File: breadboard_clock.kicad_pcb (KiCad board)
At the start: 2 copper layers, 54 x 53.5 mm, 42 parts, among them J1 Conn_01x02_Male, J2 Conn_01x03_Male, J3 USB_C_Receptacle_USB2.0, P1 1M, SW1 SW_Push, SW2 SW_SPDT, U1 ICM7555, U2 74LS04-Full, U3 74LS08-Full, U5 ICM7555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

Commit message: Add files via upload
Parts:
- added G***: LOGO, breadboard_clock-master:github_image, B.Cu at (467.5, 80.0)
- added REF**: MountingHole_2.5mm, MountingHole:MountingHole_2.5mm, F.Cu at (222.0, 78.0)
- added REF**: MountingHole_2.5mm, MountingHole:MountingHole_2.5mm, F.Cu at (222.0, 122.0)
- added REF**: MountingHole_2.5mm, MountingHole:MountingHole_2.5mm, F.Cu at (178.0, 122.0)
- added REF**: MountingHole_2.5mm, MountingHole:MountingHole_2.5mm, F.Cu at (178.0, 78.0)
- P1: footprint Potentiometer_SMD:Potentiometer_Bourns_3224X_Vertical -> Potentiometer_SMD:Potentiometer_Bourns_3314J_Vertical
- SW1: footprint Button_Switch_SMD:SW_SPST_B3S-1000 -> Button_Switch_SMD:SW_SPST_B3U-1100P-B
- moved J2 74.5 mm to (221.1, 114.5)
- moved P1 73.8 mm to (193.5, 115.5)
- moved R2 73.8 mm to (189.2, 115.6)
- moved SW1 67.6 mm to (205.5, 115.2)
- moved C8 65.0 mm to (201.9, 88.0), turned to 0 degrees
- moved U3 64.6 mm to (210.0, 82.5)
- moved C6 64.6 mm to (215.0, 81.5)
- moved D5 61.3 mm to (180.2, 88.5)
- moved C9 61.1 mm to (198.1, 88.0)
- moved C10 60.8 mm to (223.5, 88.5)
- moved U2 60.5 mm to (218.5, 89.5)
- moved D4 59.8 mm to (196.8, 99.6)
- moved C1 59.8 mm to (183.7, 105.0)
- moved C5 59.8 mm to (206.5, 102.9)
- moved D1 59.8 mm to (178.5, 99.5)
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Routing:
- net GND: track 160.8 -> 239.1 mm, vias 16 -> 20
- net CLK: track 29.1 -> 75.8 mm, vias 0 -> 2
- net VCC: track 33.3 -> 70.4 mm, vias 8 -> 13
- net Net-(D1-Pad2): track 35.9 -> 50.2 mm
- net Net-(R4-Pad2): track 39.5 -> 25.2 mm
- net Net-(D4-Pad2): track 38.2 -> 49.3 mm
- net Net-(U2-Pad6): track 14.2 -> 23.9 mm, vias 0 -> 2
- net Net-(R8-Pad2): track 24.4 -> 33.0 mm
- net Net-(C4-Pad1): track 16.7 -> 10.3 mm, vias 2 -> 0
- net ~CLK: track 58.9 -> 52.8 mm, vias 0 -> 2
- net Net-(U2-Pad2): track 21.7 -> 15.7 mm
- net Net-(R1-Pad2): track 26.9 -> 21.5 mm, vias 0 -> 2
- net Net-(U2-Pad3): track 13.0 -> 17.2 mm, vias 2 -> 0
- net Net-(U2-Pad11): track 17.0 -> 20.0 mm
- net Net-(U2-Pad4): track 10.7 -> 13.7 mm
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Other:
- board size 54 x 53.5 mm -> 50 x 50 mm
- board text added: "555 TIMER CLOCK DESIGNED BY b0xmaker github.com/b0xmaker/breadboard_clock v0: PCB CREATED 2021-06-20"
- board text added: "AND GATE"
- board text added: "AUTO CLK (.5-7 Hz)"
- board text added: "CLK ADV. (MAN)"
- board text added: "CLK SPEED (AUTO)"
- board text added: "CLK SWITCH (MAN/AUTO)"
- board text added: "INVERTER"
- board text added: "MAN CLK"
- board text added: "POWER INPUT (2-18V DC)"
- board text added: "USB C INPUT"

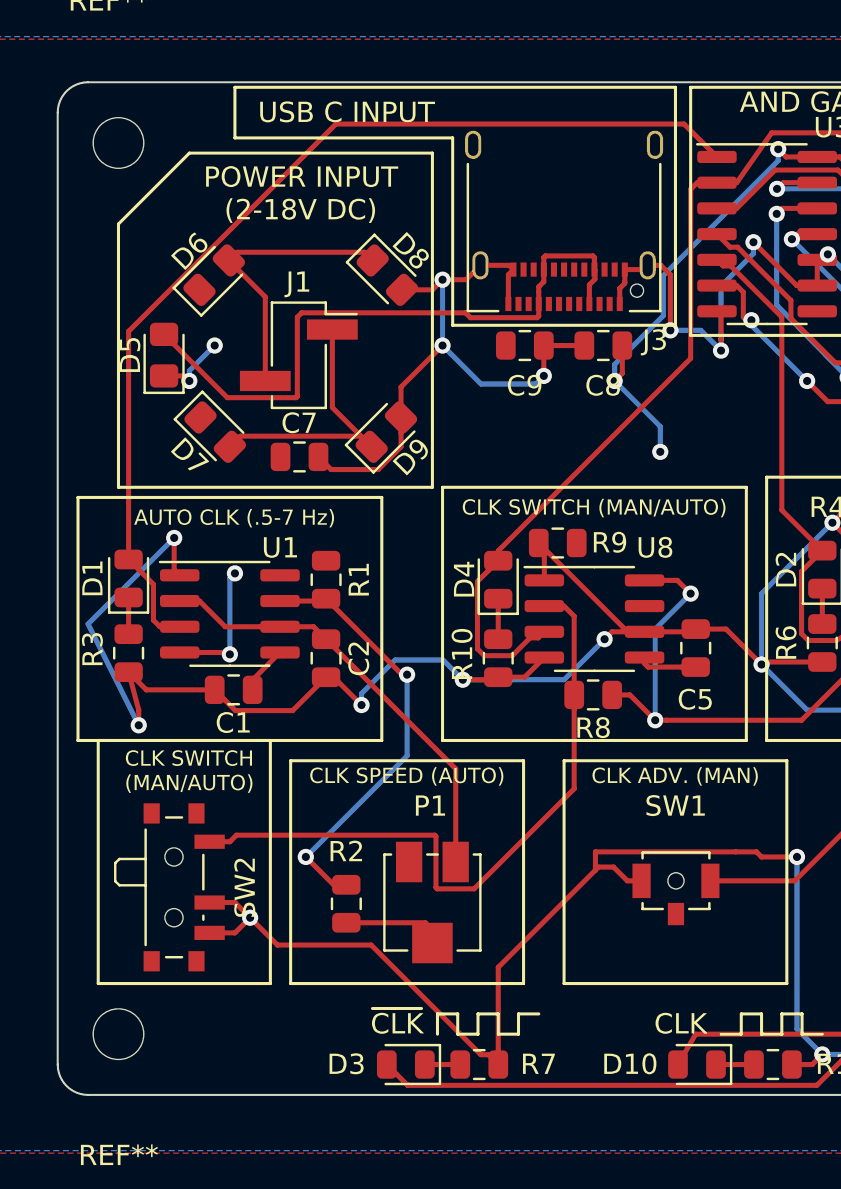
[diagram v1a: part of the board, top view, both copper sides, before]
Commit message: Add files via upload
Modified PCB/Schematic to get clock switching 555 circuit working. Trace was leading from pin 4 to GND, causing this 555 to always be in "reset" mode.
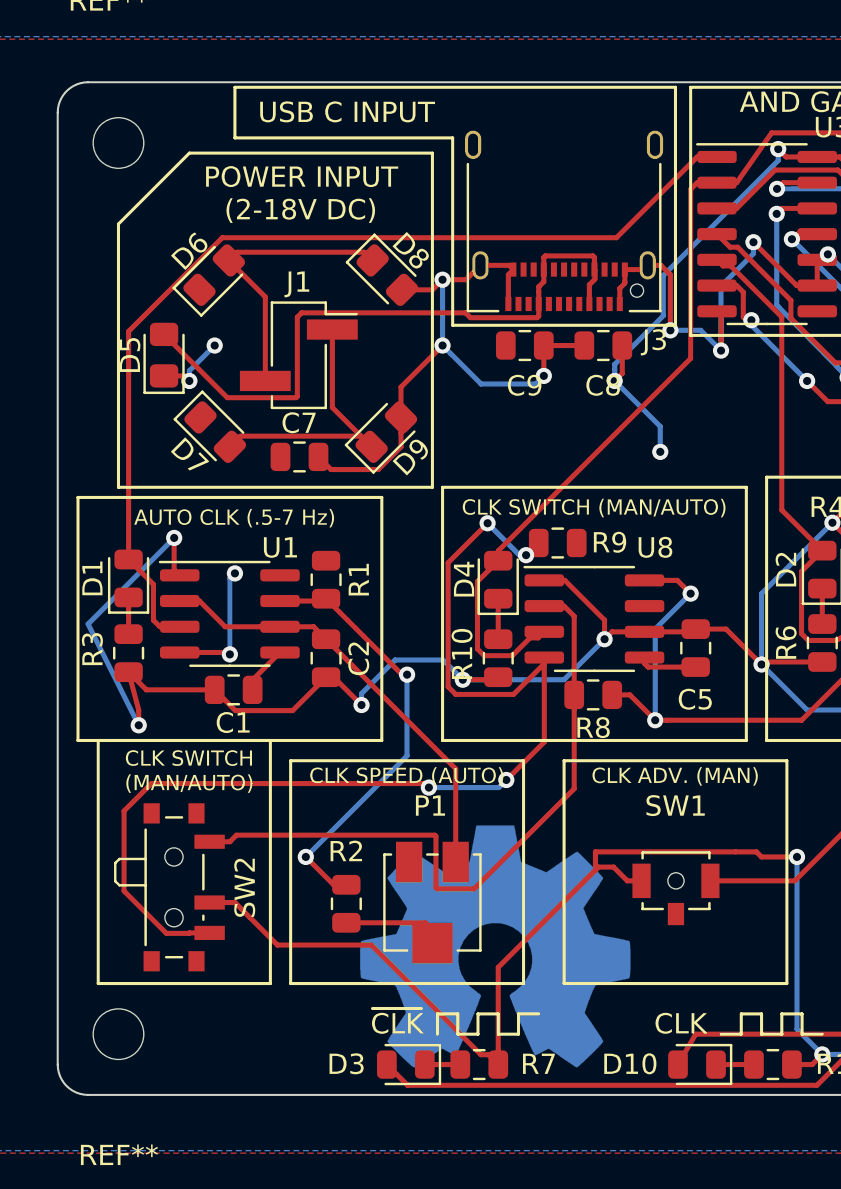
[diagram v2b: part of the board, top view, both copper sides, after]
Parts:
- added REF**: OSHW-Symbol_13.4x12mm_Copper, Symbol:OSHW-Symbol_13.4x12mm_Copper, B.Cu at (196.6, 117.7)
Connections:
- R9 pad 2: GND -> Net-(R9-Pad2)
- SW2 pad 3: GND -> Net-(R9-Pad2)
- U8 pad 4: GND -> Net-(R9-Pad2)
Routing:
- net Net-(R9-Pad2): track 0.00 -> 53.7 mm, vias 0 -> 4
- net GND: track 239.1 -> 230.6 mm, vias 20 -> 19
- net Net-(D1-Pad2): track 50.2 -> 48.8 mm
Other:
- board text added: "555 TIMER CLOCK DESIGNED BY b0xmaker github.com/b0xmaker/breadboard_clock v0: PCB CREATED 2021-06-20 v1: MOD. U8/PIN4. Removed ground cnx."
- board text removed: "555 TIMER CLOCK DESIGNED BY b0xmaker github.com/b0xmaker/breadboard_clock v0: PCB CREATED 2021-06-20"
